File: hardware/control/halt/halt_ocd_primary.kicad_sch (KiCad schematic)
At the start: 14 parts, among them U6 LM311

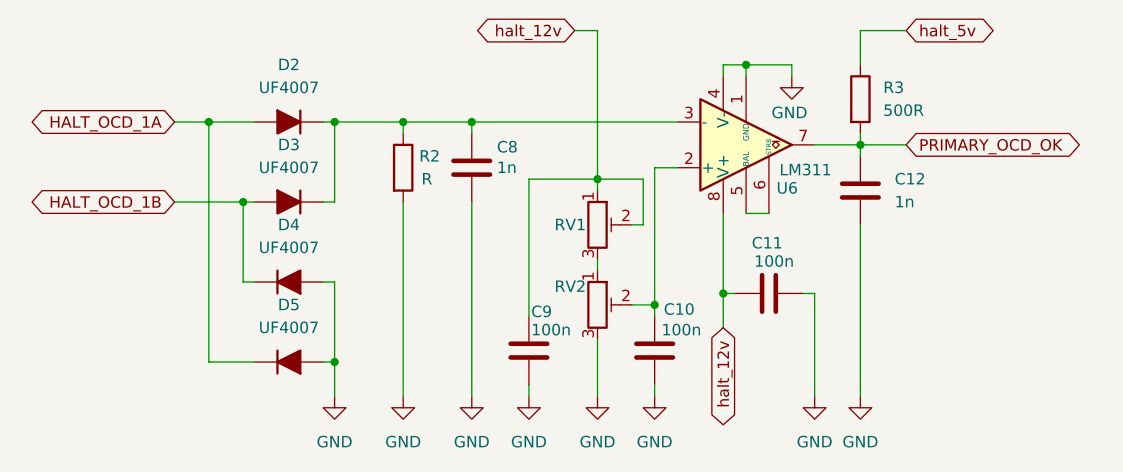
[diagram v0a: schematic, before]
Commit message: add progress on main drive controller and switch to hiearchical labels
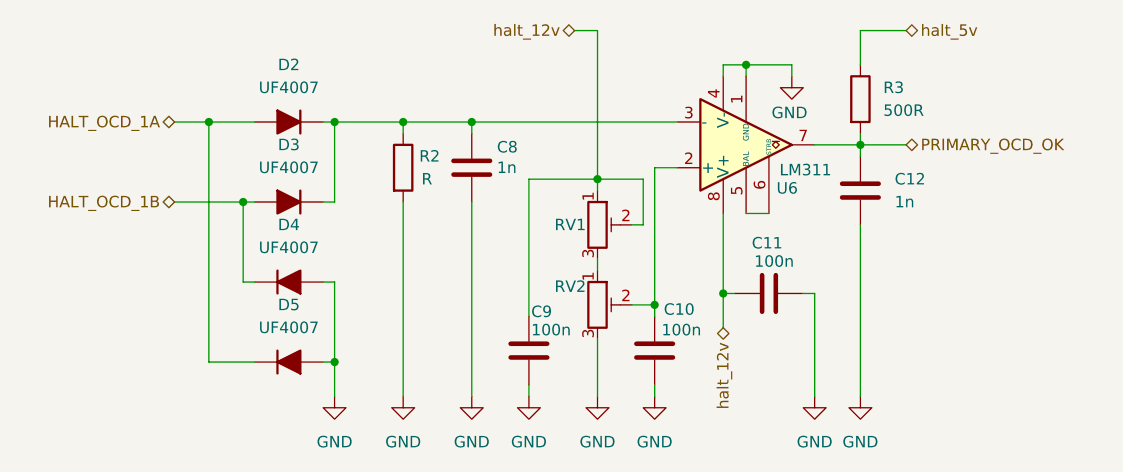
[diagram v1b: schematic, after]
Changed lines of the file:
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@@
 		)
 	)
-	(global_label "halt_12v"
+	(hierarchical_label "HALT_OCD_1B"
 		(shape bidirectional)
-		(at 143.51 81.28 180)
-		(fields_autoplaced yes)
+		(at 99.06 100.33 180)
 		(effects
 			(font
@@
 			(justify right)
 		)
-		(property "Intersheetrefs" "${INTERSHEET_REFS}"
-			(at 131.3704 81.28 0)
-			(effects
-				(font
-					(size 1.27 1.27)
-				)
-				(justify right)
-				(hide yes)
-			)
-		)
 	)
-	(global_label "HALT_OCD_1A"
+	(hierarchical_label "HALT_OCD_1A"
 		(shape bidirectional)
 		(at 99.06 91.44 180)
-		(fields_autoplaced yes)
 		(effects
 			(font
@@
 			(justify right)
 		)
-		(property "Intersheetrefs" "${INTERSHEET_REFS}"
-			(at 82.4449 91.44 0)
-			(effects
-				(font
-					(size 1.27 1.27)
-				)
-				(justify right)
-				(hide yes)
-			)
-		)
 	)
-	(global_label "PRIMARY_OCD_OK"
+	(hierarchical_label "PRIMARY_OCD_OK"
 		(shape bidirectional)
 		(at 180.34 93.98 0)
-		(fields_autoplaced yes)
 		(effects
 			(font
@@
 			(justify left)
 		)
-		(property "Intersheetrefs" "${INTERSHEET_REFS}"
-			(at 200.8861 93.98 0)
-			(effects
-				(font
-					(size 1.27 1.27)
-				)
-				(justify left)
-				(hide yes)
+	)
+	(hierarchical_label "halt_5v"
+		(shape bidirectional)
+		(at 180.34 81.28 0)
+		(effects
+			(font
+				(size 1.27 1.27)
 			)
+			(justify left)
 		)
 	)
-	(global_label "halt_12v"
+	(hierarchical_label "halt_12v"
 		(shape bidirectional)
 		(at 160.02 114.3 270)
-		(fields_autoplaced yes)
 		(effects
 			(font
@@
 			(justify right)
 		)
-		(property "Intersheetrefs" "${INTERSHEET_REFS}"
-			(at 160.02 126.4396 90)
-			(effects
-				(font
-					(size 1.27 1.27)
-				)
-				(justify right)
-				(hide yes)
-			)
-		)
 	)
-	(global_label "halt_5v"
+	(hierarchical_label "halt_12v"
 		(shape bidirectional)
-		(at 180.34 81.28 0)
-		(fields_autoplaced yes)
-		(effects
-			(font
-				(size 1.27 1.27)
-			)
-			(justify left)
-		)
-		(property "Intersheetrefs" "${INTERSHEET_REFS}"
-			(at 191.2701 81.28 0)
-			(effects
-				(font
-					(size 1.27 1.27)
-				)
-				(justify left)
-				(hide yes)
-			)
-		)
-	)
-	(global_label "HALT_OCD_1B"
-		(shape bidirectional)
-		(at 99.06 100.33 180)
-		(fields_autoplaced yes)
+		(at 143.51 81.28 180)
 		(effects
 			(font
@@
 			(justify right)
 		)
-		(property "Intersheetrefs" "${INTERSHEET_REFS}"
-			(at 82.2635 100.33 0)
-			(effects
-				(font
-					(size 1.27 1.27)
-				)
-				(justify right)
-				(hide yes)
-			)
-		)
 	)

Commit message: update right about freaking everything
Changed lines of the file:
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@@
 	(wire
 		(pts
-			(xy 162.56 101.6) (xy 165.1 101.6)
+			(xy 162.56 102.87) (xy 165.1 102.87)
 		)
 		(stroke
@@
 	(wire
 		(pts
+			(xy 162.56 102.87) (xy 162.56 101.6)
+		)
+		(stroke
+			(width 0)
+			(type default)
+		)
+	)
+	(wire
+		(pts
 			(xy 170.18 110.49) (xy 168.91 110.49)
 		)
@@
 		)
 		(stroke
+			(width 0)
+			(type default)
+		)
+	)
+	(wire
+		(pts
+			(xy 165.1 102.87) (xy 165.1 101.6)
+		)
+		(stroke
